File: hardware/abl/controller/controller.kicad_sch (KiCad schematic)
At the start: 38 parts, among them IC2 FXL6408UMX, IC3 VEML6040A3OG, IC4 FXL6408UMX, J1 SFW20S-2STE1LF, J2 Conn_02x05_Odd_Even, J3 Conn_02x05_Odd_Even, J4 PRT-14417, J5 Conn_02x05_Odd_Even, Q2 AO3401A, Q4 AO3401A, U1 INA219AxD, U2 TXB0104RUT

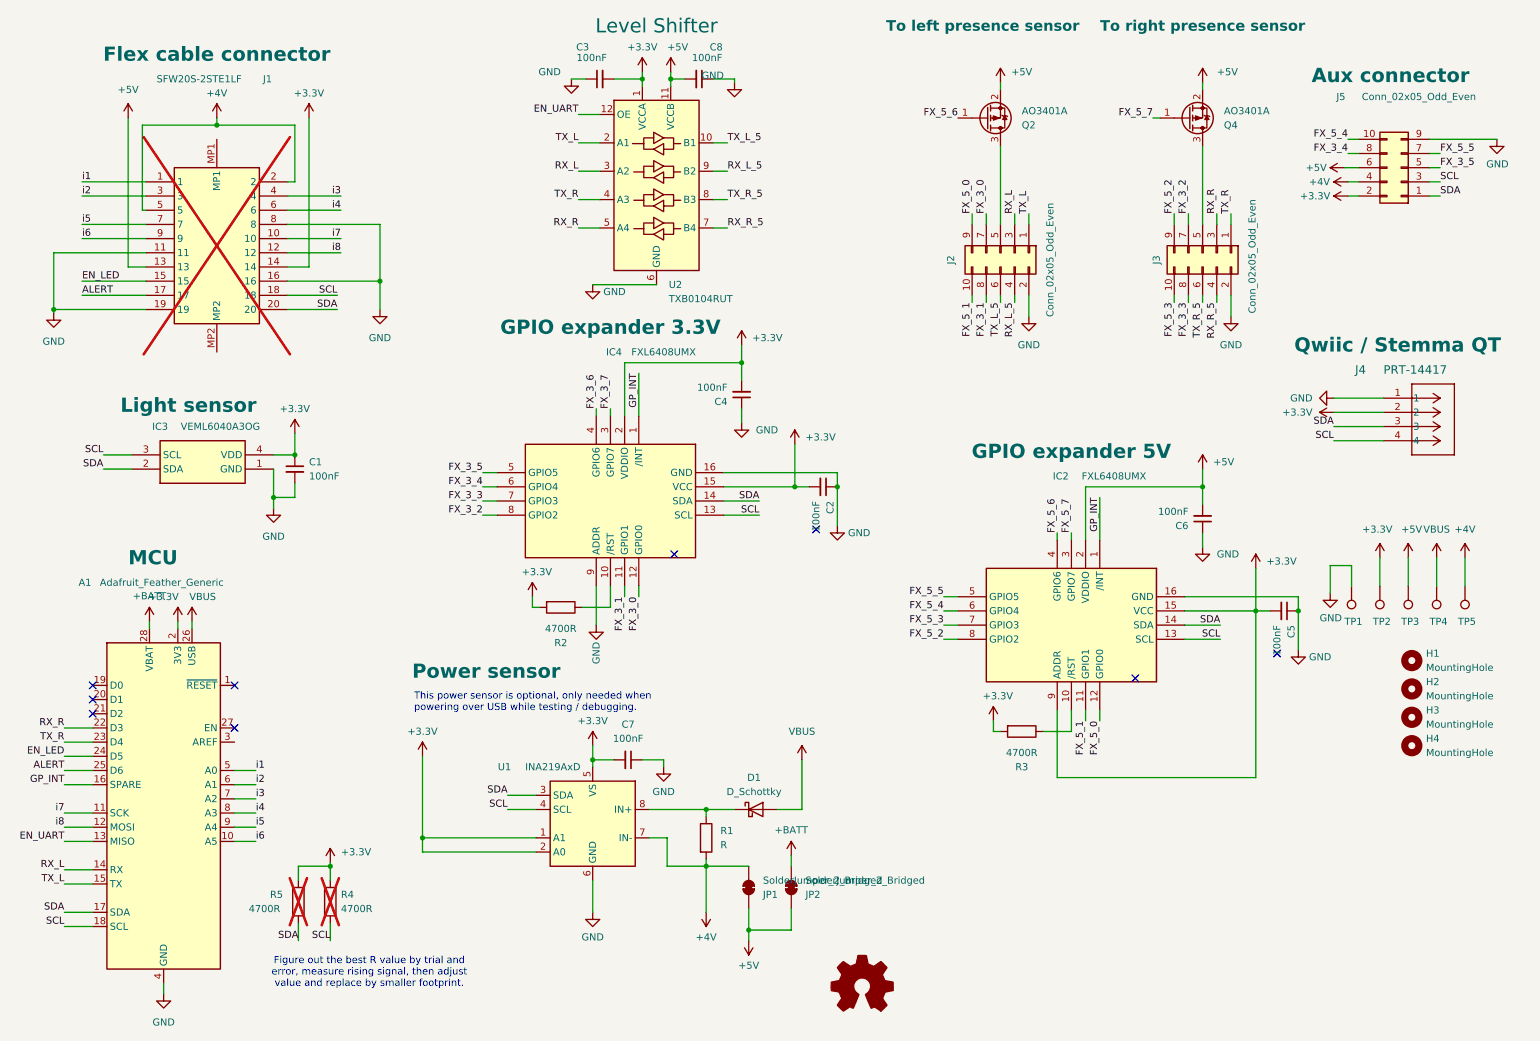
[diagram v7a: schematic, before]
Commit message: Change pins 13 and 16 to fix bootloader problem. Nees better docu.
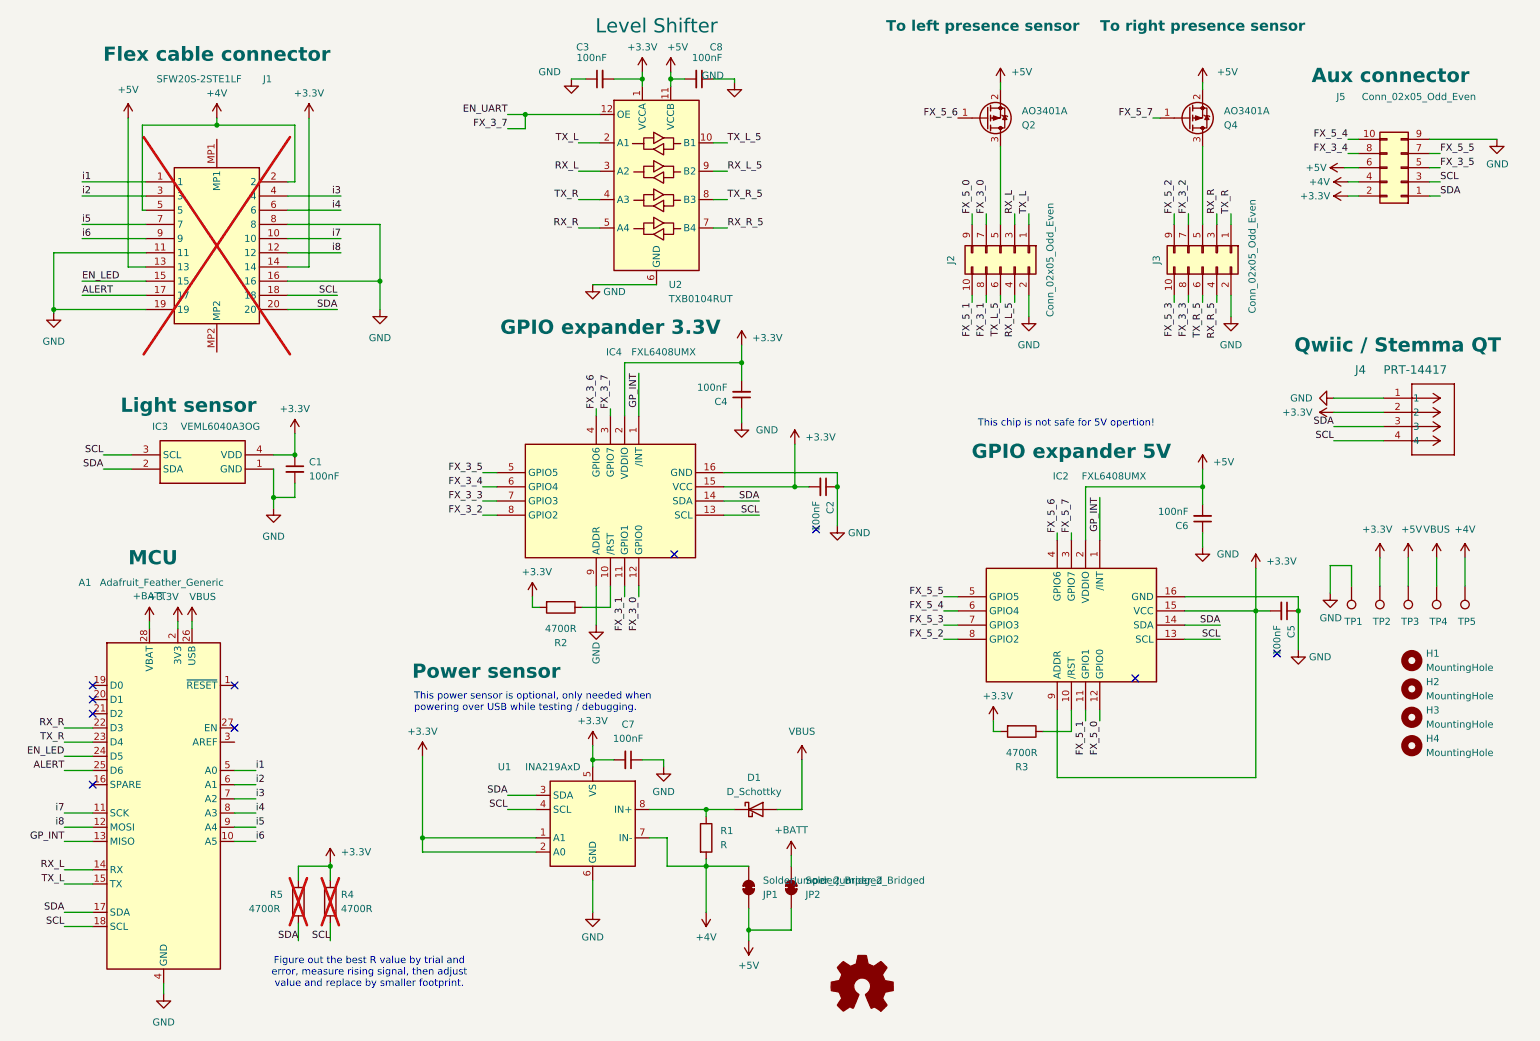
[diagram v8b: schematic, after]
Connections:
- net FX_3_7 is gone; now on net EN_UART: IC4.3 (GPIO7)
- net EN_UART: no longer A1.13 (MISO)
- net GP_INT: now also A1.13 (MISO); no longer A1.16 (SPARE)
- no-connect marks 9 -> 10
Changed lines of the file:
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@@
+	)
+	(junction
+		(at 106.045 33.02)
+		(diameter 0)
+		(color 0 0 0 0)
 	)
 	(junction
@@
 		(at 158.115 107.315)
 	)
+	(no_connect
+		(at 28.575 153.035)
+	)
 	(wire
 		(pts
@@
 	(wire
 		(pts
+			(xy 106.045 33.02) (xy 106.045 35.56)
+		)
+		(stroke
+			(width 0)
+			(type default)
+		)
+	)
+	(wire
+		(pts
 			(xy 123.825 77.47) (xy 123.825 86.995)
 		)
@@
 	(wire
 		(pts
+			(xy 106.045 33.02) (xy 119.38 33.02)
+		)
+		(stroke
+			(width 0)
+			(type default)
+		)
+	)
+	(wire
+		(pts
 			(xy 224.79 50.8) (xy 224.79 52.705)
 		)
@@
 	(wire
 		(pts
-			(xy 23.495 153.035) (xy 28.575 153.035)
-		)
-		(stroke
-			(width 0)
-			(type default)
-		)
-	)
-	(wire
-		(pts
 			(xy 236.855 121.92) (xy 224.155 121.92)
 		)
@@
 	(wire
 		(pts
-			(xy 115.57 33.02) (xy 119.38 33.02)
+			(xy 102.87 33.02) (xy 106.045 33.02)
 		)
 		(stroke
@@
 	(wire
 		(pts
+			(xy 106.045 35.56) (xy 102.87 35.56)
+		)
+		(stroke
+			(width 0)
+			(type default)
+		)
+	)
+	(wire
+		(pts
 			(xy 115.57 53.34) (xy 119.38 53.34)
 		)
@@
 			(width 0)
 			(type default)
+		)
+	)
+	(text_box "This chip is not safe for 5V opertion!"
+		(exclude_from_sim no)
+		(at 186.055 86.36 0)
+		(size 39.37 3.81)
+		(stroke
+			(width -0.0001)
+			(type default)
+		)
+		(fill
+			(type none)
+		)
+		(effects
+			(font
+				(size 1.27 1.27)
+				(color 255 54 79 1)
+			)
+			(justify left top)
 		)
 	)
@@
 	)
 	(label "EN_UART"
-		(at 115.57 33.02 180)
+		(at 102.87 33.02 180)
 		(fields_autoplaced yes)
 		(effects
@@
 	)
 	(label "GP_INT"
-		(at 23.495 153.035 180)
+		(at 23.495 163.195 180)
 		(fields_autoplaced yes)
 		(effects
@@
 		)
 	)
-	(label "EN_UART"
-		(at 23.495 163.195 180)
-		(fields_autoplaced yes)
-		(effects
-			(font
-				(size 1.27 1.27)
-			)
-			(justify right bottom)
-		)
-	)
 	(label "SCL"
 		(at 30.48 93.98 180)
@@
 		(fields_autoplaced yes)
 		(effects
+			(font
+				(size 1.27 1.27)
+			)
+			(justify right bottom)
+		)
+	)
+	(label "FX_3_7"
+		(at 102.87 35.56 180)
+		(fields_autoplaced yes)
+		(effects
